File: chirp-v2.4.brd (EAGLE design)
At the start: 141.4 x 16.8 mm, 19 parts, among them IC1 TINY24/44/84-SSU, SW1 SPST_TACTFSMJSMA

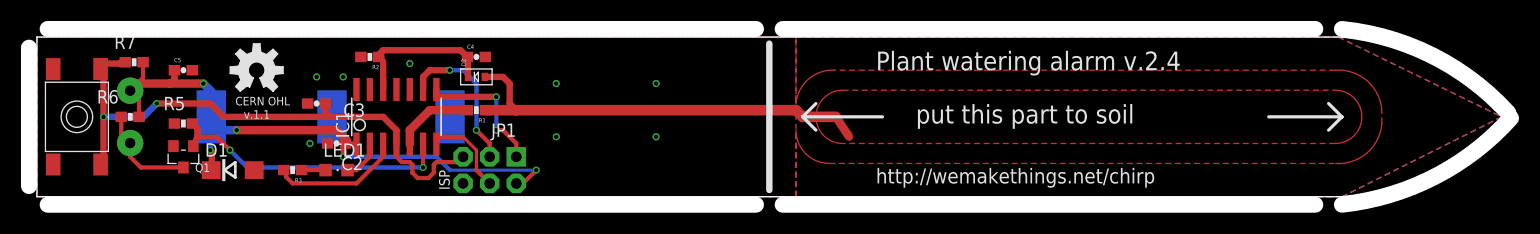
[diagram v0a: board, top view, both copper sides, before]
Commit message: Silk changes
Removed Chirp labels
Added Watric labels
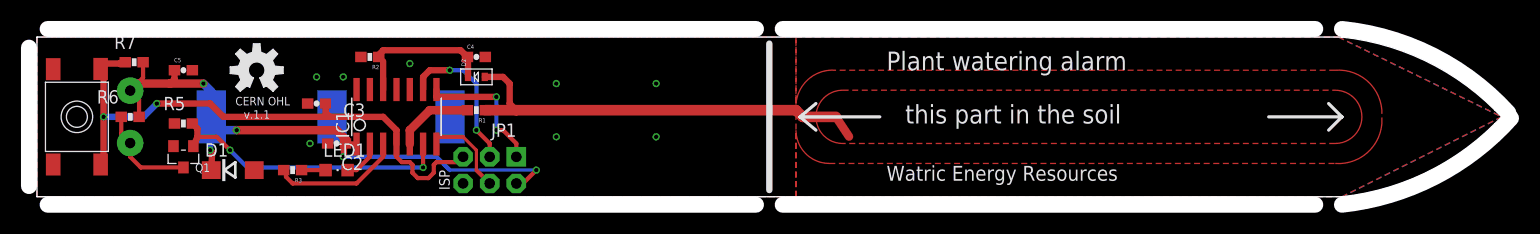
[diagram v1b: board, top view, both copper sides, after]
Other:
- board text added: "Plant watering alarm"
- board text added: "Thirsty!"
- board text added: "Watric Energy Resources"
- board text added: "this part in the soil"
- board text removed: "Plant watering alarm v.2.4"
- board text removed: "chirp!"
- board text removed: "http://wemakethings.net/chirp"
- board text removed: "put this part to soil"
